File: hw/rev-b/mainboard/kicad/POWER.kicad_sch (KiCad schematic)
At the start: 65 parts, among them J10 5V PWR, J11 9V POWER, J13 9V POWER JACK, J27 6V POWER, J8 PET POWER, U3 AMS1117-3.3, U4 LM317AG-TN3-R, U5 LM317AG-TN3-R, U6 TPS5430DDA

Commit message: chore(hw): move 330uF to C7, make footprint accept P5.00 leads
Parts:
- C7: value 11000u -> 330uF; footprint EconoPET:CP_Radial_D16.0mm_P7.50mm -> EconoPET:CP_Radial_D16.0mm_P5.00mm_P7.50mm; MOUSER 661-BV250L113AL40S -> 667-EEU-FM1V331; now fitted
- C89: now not fitted
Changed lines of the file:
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@@
 		(in_bom yes)
 		(on_board yes)
-		(dnp yes)
+		(dnp no)
 		(property "Reference" "C7"
 			(at 74.6252 40.7416 0)
@@
 			)
 		)
-		(property "Value" "11000u"
+		(property "Value" "330uF"
 			(at 74.6252 43.053 0)
 			(effects
@@
 			)
 		)
-		(property "Footprint" "EconoPET:CP_Radial_D16.0mm_P7.50mm"
+		(property "Footprint" "EconoPET:CP_Radial_D16.0mm_P5.00mm_P7.50mm"
 			(at 72.39 41.91 0)
 			(effects
@@
 			)
 		)
-		(property "Datasheet" "https://www.chemi-con.co.jp/products/relatedfiles/capacitor/catalog/LBVLL-e.PDF"
+		(property "Datasheet" "https://industrial.panasonic.com/cdbs/www-data/pdf/RDF0000/ABA0000C1018.pdf"
 			(at 72.39 41.91 0)
 			(effects
@@
 			)
 		)
-		(property "MOUSER" "661-BV250L113AL40S"
+		(property "MOUSER" "667-EEU-FM1V331"
 			(at 72.39 41.91 0)
 			(effects
@@
 		(in_bom yes)
 		(on_board yes)
-		(dnp no)
+		(dnp yes)
 		(property "Reference" "C89"
 			(at 61.9252 40.7416 0)

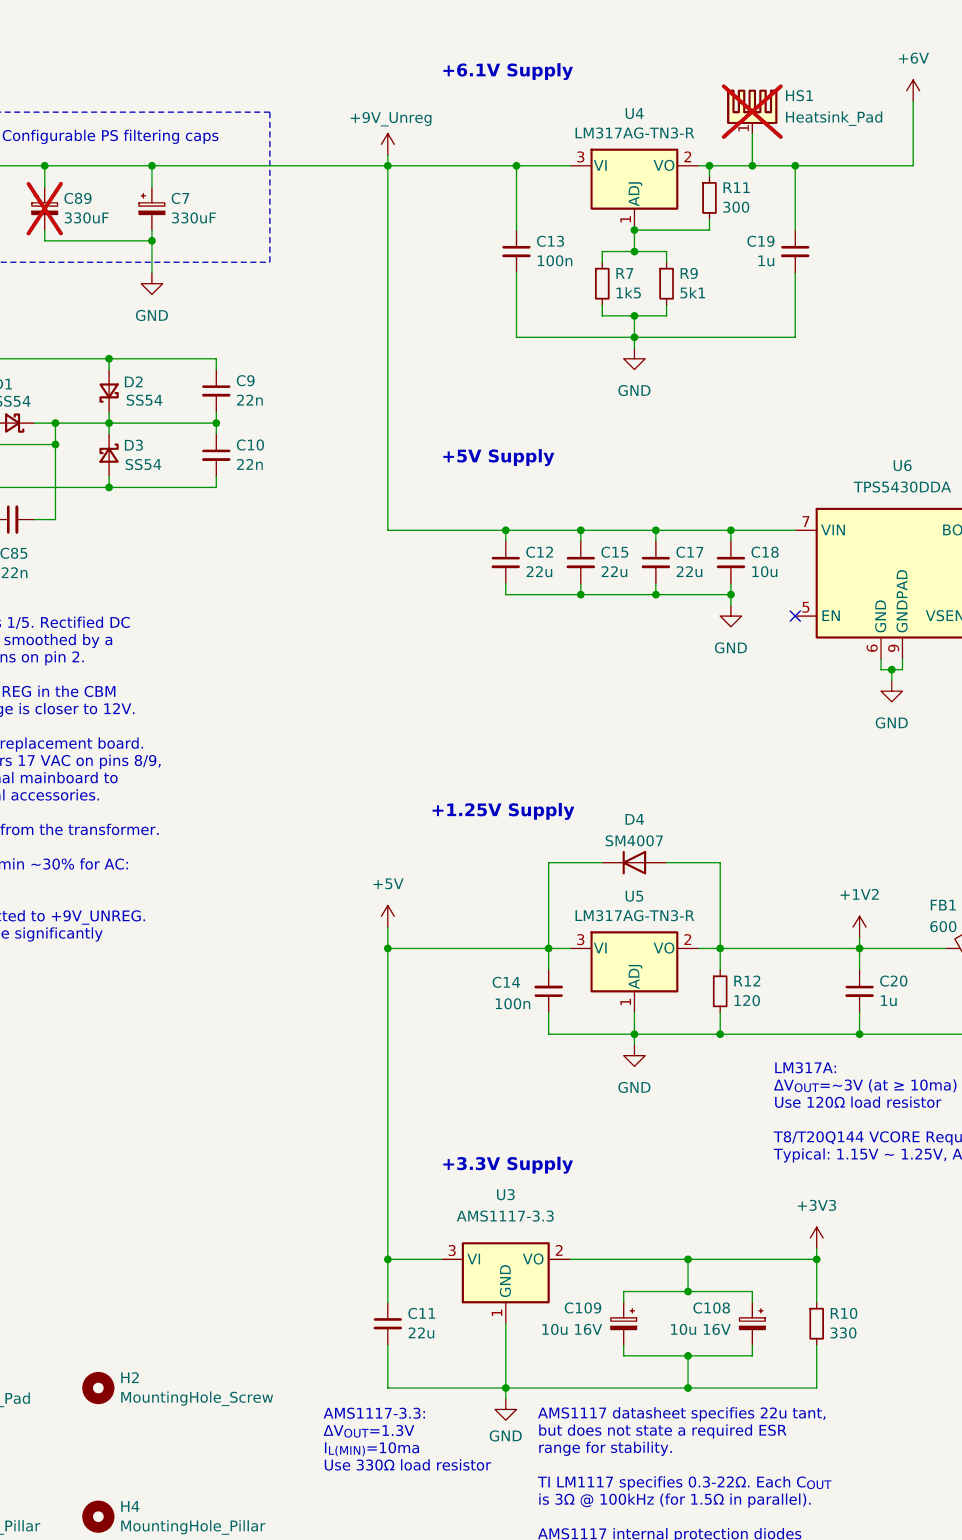
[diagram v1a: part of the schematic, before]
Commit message: chore(hw): add 2 addtl caps on buck VIN, rotate 9V pin header
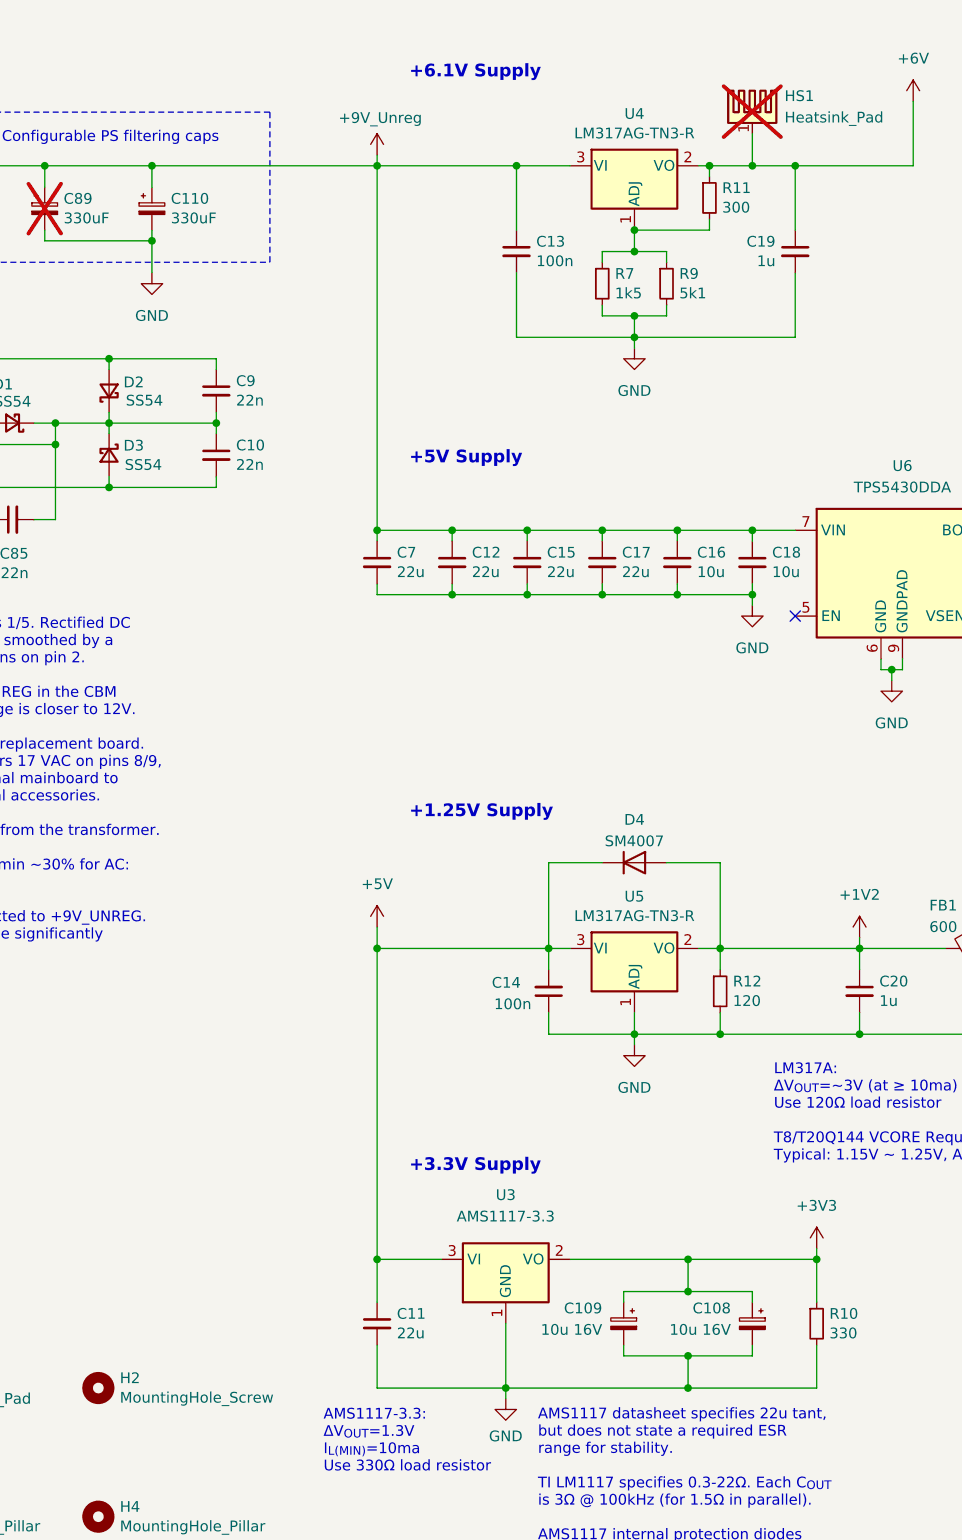
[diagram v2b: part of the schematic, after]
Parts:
- added C16: 10u, Capacitor_SMD:C_0603_1608Metric, symbol Device:C_Small
- added C7: 22u, Capacitor_SMD:C_0805_2012Metric, symbol Device:C_Small
- renumbered C7 to C110
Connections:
- net +9V_Unreg: now also C16.1, C7.1
- net GND: now also C16.2, C7.2
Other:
- moved on the sheet: C11, C12, C15, C17, C18

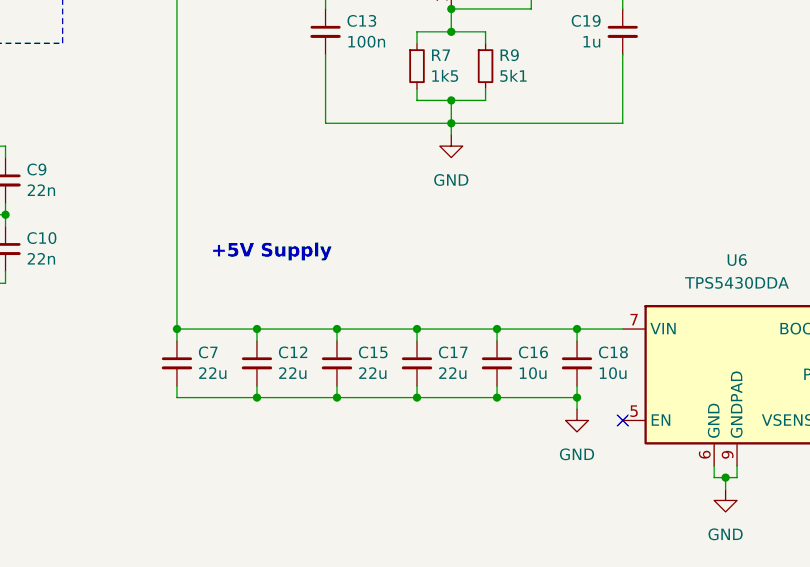
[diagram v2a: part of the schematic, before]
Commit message: feat(hw): additional mlcc caps on rectified AC
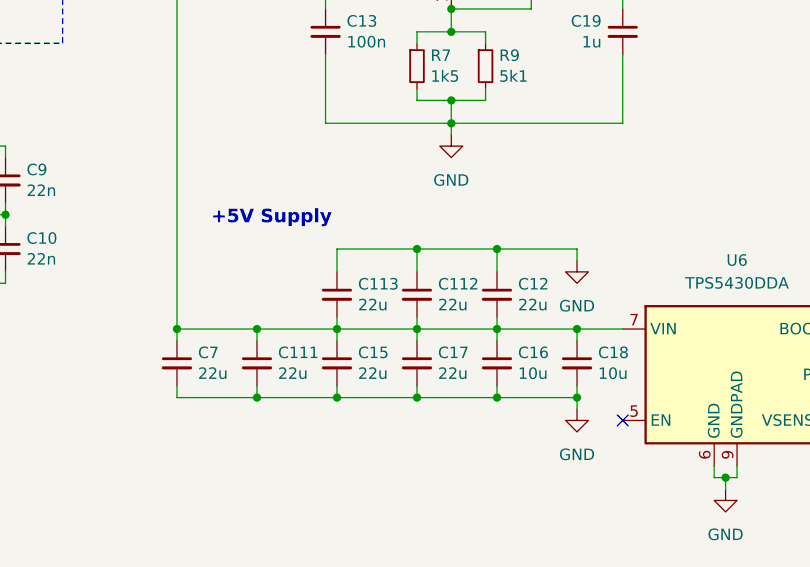
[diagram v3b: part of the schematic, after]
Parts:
- added C112, C113, C12: 22u, Capacitor_SMD:C_0805_2012Metric, symbol Device:C_Small
- renumbered C12 to C111
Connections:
- net +9V_Unreg: now also C112.2, C113.2, C12.2
- net GND: now also C112.1, C113.1, C12.1

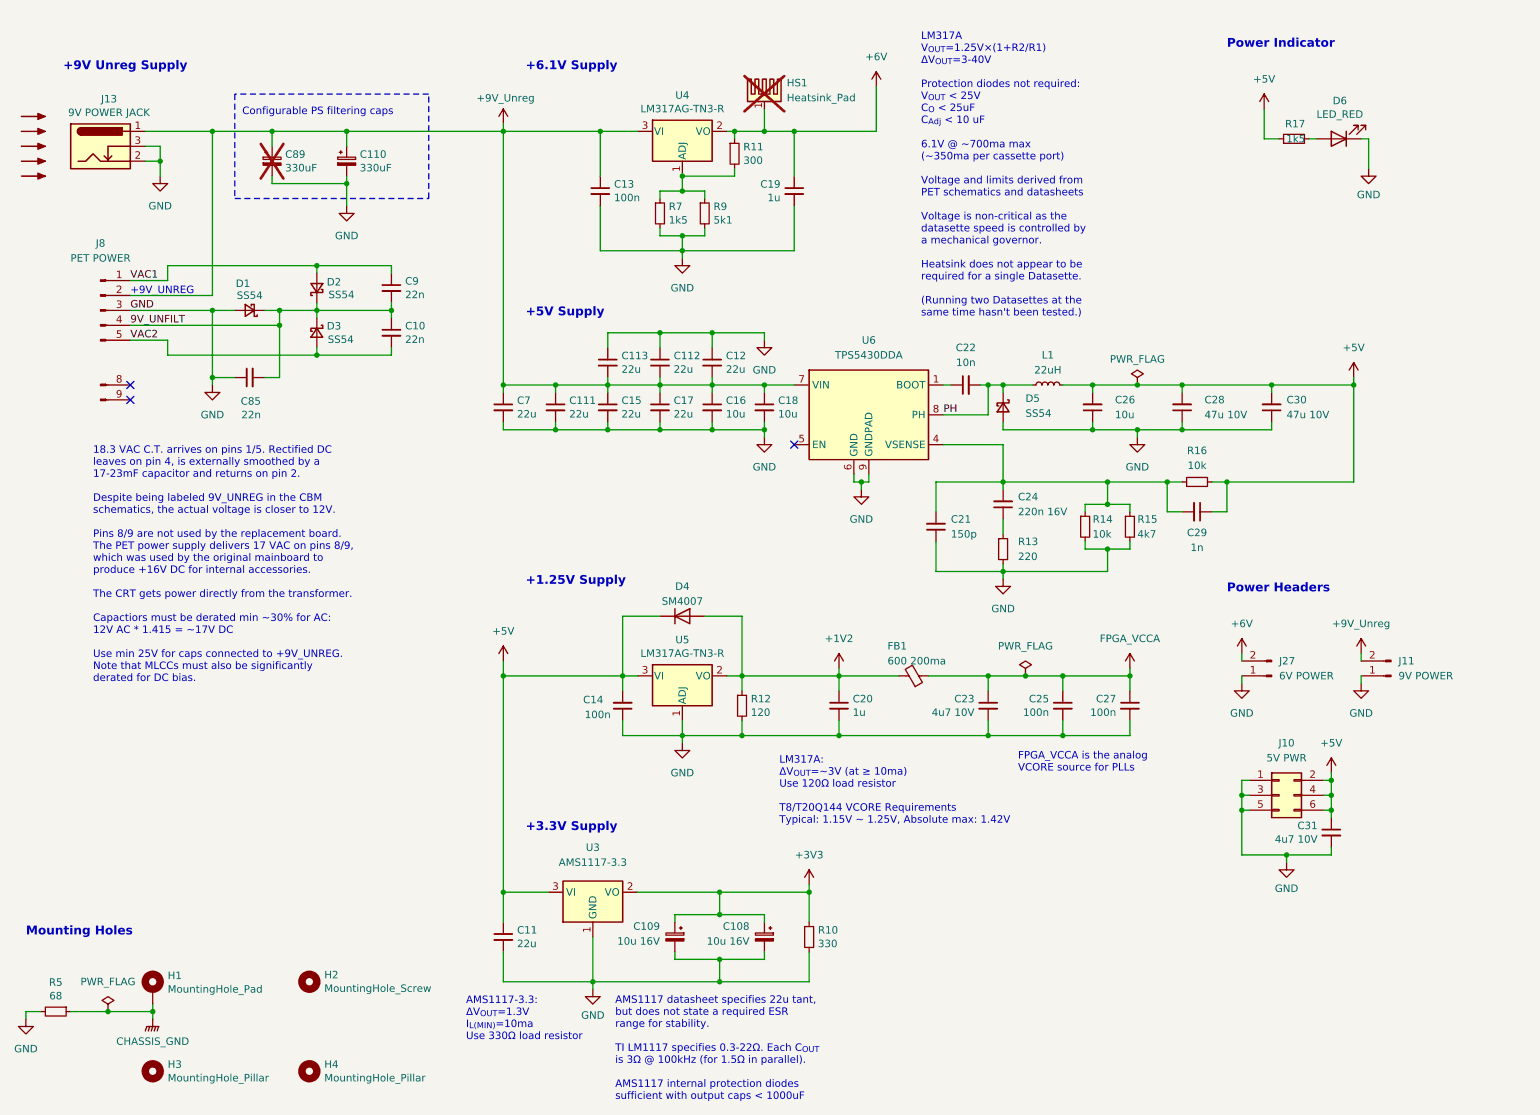
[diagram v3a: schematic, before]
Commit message: hw: use TPS5430 for 6V supply
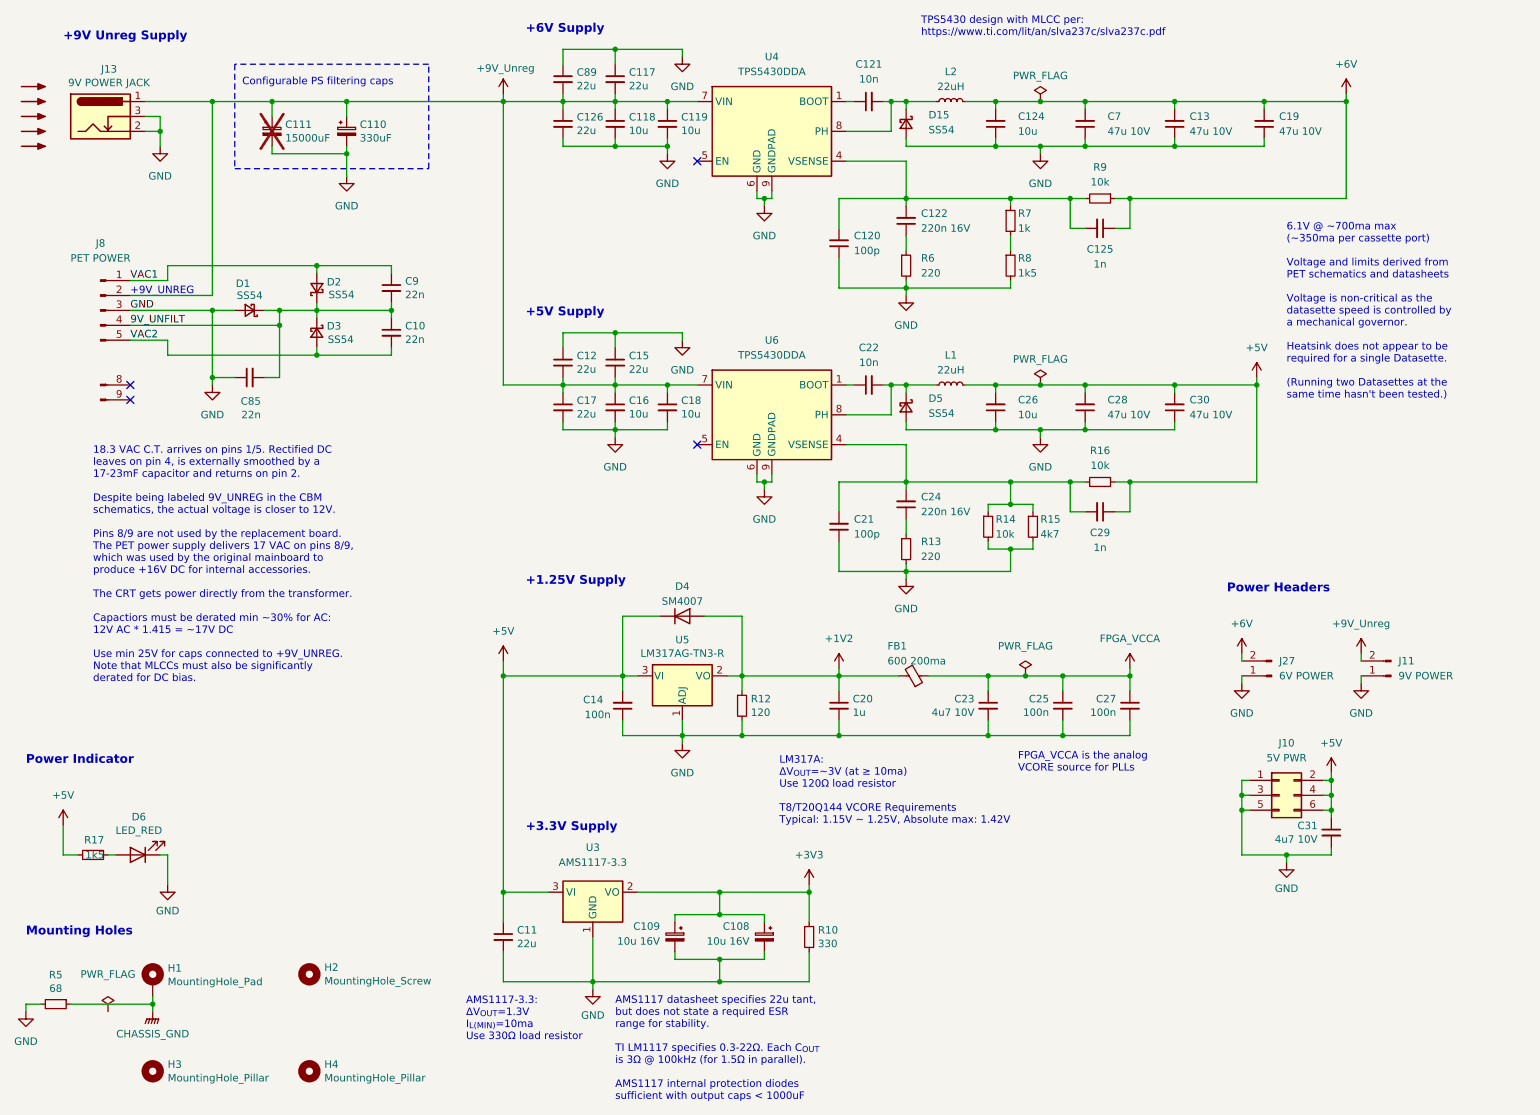
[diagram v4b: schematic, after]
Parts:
- removed C112, C113, C12: 22u, Capacitor_SMD:C_0805_2012Metric, symbol Device:C_Small
- removed C89: 330uF, EconoPET:CP_Radial_D24.0mm_P5.00mm_P7.50mm_P10.00mm_SnapIn, symbol Device:C_Polarized_Small
- removed HS1: Heatsink_Pad, PET:V1100SMDBL_or_573100D00000G, symbol Mechanical:Heatsink_Pad
- removed R11: 300, Resistor_SMD:R_0402_1005Metric, symbol Device:R_Small
- removed U4: LM317AG-TN3-R, Package_TO_SOT_SMD:TO-252-2, symbol Regulator_Linear:LM317_TO-252
- added C111: 15000uF, EconoPET:CP_Radial_D18.0mm_P5.00mm_P7.50mm, symbol Device:C_Polarized_Small
- added C117, C126, C89: 22u, Capacitor_SMD:C_0805_2012Metric, symbol Device:C_Small
- added C118, C119, C124: 10u, Capacitor_SMD:C_0603_1608Metric, symbol Device:C_Small
- added C120: 100p, Capacitor_SMD:C_0402_1005Metric, symbol Device:C_Small
- added C121: 10n, Capacitor_SMD:C_0402_1005Metric, symbol Device:C_Small
- added C122: 220n 16V, Capacitor_SMD:C_0402_1005Metric, symbol Device:C_Small
- added C125: 1n, Capacitor_SMD:C_0402_1005Metric, symbol Device:C_Small
- added D15: SS54, Diode_SMD:D_SMA, symbol Device:D_Schottky_Small
- added L2: 22uH, JLCPCB:IND-SMD_L12.5-W12.5, symbol Device:L_Small
- added R6: 220, Resistor_SMD:R_0402_1005Metric, symbol Device:R_Small
- added R8: 1k5, Resistor_SMD:R_0402_1005Metric, symbol Device:R_Small
- added U4: TPS5430DDA, EconoPET:TI_SO-PowerPAD-8_ThermalVias, symbol Regulator_Switching:TPS5430DDA
- C110: footprint EconoPET:CP_Radial_D16.0mm_P5.00mm_P7.50mm -> EconoPET:CP_Radial_D12.5mm_P5.00mm_P7.50mm
- C13: value 100n -> 47u 10V; footprint Capacitor_SMD:C_0402_1005Metric -> Capacitor_SMD:C_1206_3216Metric; LCSC C307331 -> C96123
- C19: value 1u -> 47u 10V; footprint Capacitor_SMD:C_0402_1005Metric -> Capacitor_SMD:C_1206_3216Metric; LCSC C52923 -> C96123
- C21: value 150p -> 100p; LCSC C1527 -> C1546
- C7: value 22u -> 47u 10V; footprint Capacitor_SMD:C_0805_2012Metric -> Capacitor_SMD:C_1206_3216Metric; LCSC C45783 -> C96123
- R7: value 1k5 -> 1k; LCSC C25867 -> C11702
- R9: value 5k1 -> 10k; LCSC C25905 -> C25744
- renumbered C111 to C12
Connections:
- net +6V: now also C13.2, C19.2, C7.2, R9.1, C124.2, C125.1, L2.2; no longer C19.1
- net +9V_Unreg: now also C12.2, C15.2, C111.1, C117.2, C118.1, C119.1, C126.1, C89.2, U4.7 (VIN); no longer C12.1, C13.1, C15.1, C7.1
- net GND: now also C12.1, C13.1, C15.1, C19.1, C7.1, C111.2, C117.1, C118.2, C119.2, C120.1, C124.1, C126.2, C89.1, D15.2 (A), R6.2, R8.2, U4.6 (GND), U4.9 (GNDPAD); no longer C12.2, C13.2, C15.2, C19.2, C7.2, R7.2, R9.2
- net at R7.1: now also R9.2, C120.2, C122.2, C125.2, U4.4 (VSENSE); no longer R9.1
- net PH: no longer names the net of C22.2, D5.1 (K), L1.1, U6.8 (PH)
- new net: C121.1, U4.1 (BOOT)
- new net: C121.2, D15.1 (K), L2.1, U4.8 (PH)
- new net: C122.1, R6.1
- new net: R7.2, R8.1
- no-connect marks 3 -> 4
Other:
- note added: "+6V Supply"
- note added: "TPS5430 design with MLCC per: https://www.ti.com/lit/an/slva237c/slva237c.pdf"
- note removed: "+6.1V Supply"
- note removed: "LM317A V_{OUT}=1.25V×(1+R2/R1) ΔV_{OUT}=3-40V Protection diodes not required: V_{OUT} < 25V C_{O} < 25uF C_{Adj} < 10 uF"
- moved on the sheet: C110, C12, C15, C16, C18, C21, C22, C24, C26, C28, C29, C30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

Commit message: hw: touchups
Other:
- note added: "Max load of ~400ma observed with a black C2N when motor is stalled at end-of-tape during rewind. 6.1V @ 1A allows 400ma per cassette port with some headroom. Voltage is non-critical as the datasette speed is controlled by a mechanical governor."
- note added: "TPS5430 design using MLCC per: https://www.ti.com/lit/an/slva237c/slva237c.pdf"
- note removed: "6.1V @ ~700ma max (~350ma per cassette port) Voltage and limits derived from PET schematics and datasheets Voltage is non-critical as the datasette speed is controlled by a mechanical governor. Heatsink does not appear to be required for a single Datasette. (Running two Datasettes at the same time hasn't been tested.)"
- note removed: "TPS5430 design with MLCC per: https://www.ti.com/lit/an/slva237c/slva237c.pdf"
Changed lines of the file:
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@@
 		)
 	)
-	(text "TPS5430 design with MLCC per:\nhttps://www.ti.com/lit/an/slva237c/slva237c.pdf"
+	(text "TPS5430 design using MLCC per:\nhttps://www.ti.com/lit/an/slva237c/slva237c.pdf"
 		(exclude_from_sim no)
 		(at 170.18 19.05 0)
@@
 		)
 	)
-	(text "6.1V @ ~700ma max\n(~350ma per cassette port)\n\nVoltage and limits derived from\nPET schematics and datasheets\n\nVoltage is non-critical as the\ndatasette speed is controlled by\na mechanical governor.\n\nHeatsink does not appear to be\nrequired for a single Datasette.\n\n(Running two Datasettes at the\nsame time hasn't been tested.)\n"
+	(text "Max load of ~400ma observed\nwith a black C2N when motor is\nstalled at end-of-tape during\nrewind.\n\n6.1V @ 1A allows 400ma per\ncassette port with some headroom.\n\nVoltage is non-critical as the\ndatasette speed is controlled by\na mechanical governor."
 		(exclude_from_sim no)
-		(at 232.41 82.55 0)
+		(at 232.41 73.66 0)
 		(effects
 			(font
